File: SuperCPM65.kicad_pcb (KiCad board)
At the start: 2 copper layers, 98.5 x 79.5 mm, 36 parts, among them CON1 db_vgparts_SNES-EDGE, J1 GSD090012SEU, J2 Mini-DIN-6, J3 Conn_01x06, U1 TXB0104D, U2 W65C22NxP, U3 AP2205-33W5-7, U4 74HC14, U5 74HC595, U6 74HC595, U8 PIC12F629-IP, U9 SST39SF010

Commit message: Routing updates
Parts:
- moved C5 2.12 mm to (66.9, 70.2), turned to -90 degrees
- moved C12 0.96 mm to (83.3, 94.3), turned to -90 degrees
- moved D5 0.60 mm to (130.7, 76.7)
- moved R6 0.40 mm to (125.8, 86.3)
- moved D4 0.30 mm to (130.6, 87.3)
- moved D3 0.25 mm to (130.5, 83.5)
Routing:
- net +5V: track 0.00 -> 362.0 mm, vias 0 -> 14
- net /BA1: track 0.00 -> 101.2 mm, vias 0 -> 6
- net ~{WR}: track 0.00 -> 91.9 mm, vias 0 -> 3
- net CLK: track 0.00 -> 91.6 mm, vias 0 -> 3
- net ~{IRQ}: track 0.00 -> 79.6 mm, vias 0 -> 2
- net ~{CE_VIA}: track 0.00 -> 71.5 mm, vias 0 -> 2
- net ~{RES}: track 0.00 -> 66.0 mm, vias 0 -> 2
- net ~{CART}: track 0.00 -> 60.0 mm, vias 0 -> 3
- net /KB_DATA: track 0.00 -> 53.8 mm, vias 0 -> 2
- net /SPI_CS: track 0.00 -> 51.4 mm, vias 0 -> 2
- net /SCK: track 0.00 -> 48.0 mm, vias 0 -> 2
- net Net-(U5-SRCLK): track 0.00 -> 47.9 mm, vias 0 -> 3
- net ~{RD}: track 0.00 -> 46.4 mm, vias 0 -> 2
- net /MOSI: track 0.00 -> 44.1 mm, vias 0 -> 2
- net /MISO: track 0.00 -> 44.0 mm, vias 0 -> 2
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- added copper zone on B.Cu, net GND
- added copper zone on F.Cu, net GND

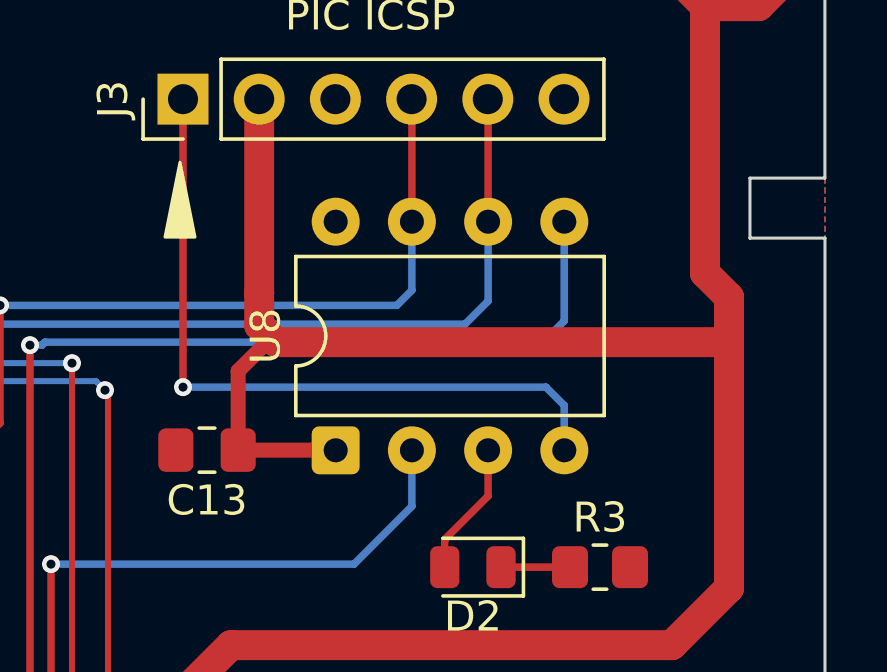
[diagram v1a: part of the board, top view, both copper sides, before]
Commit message: Fixed some 3D model issues and socketed the PIC
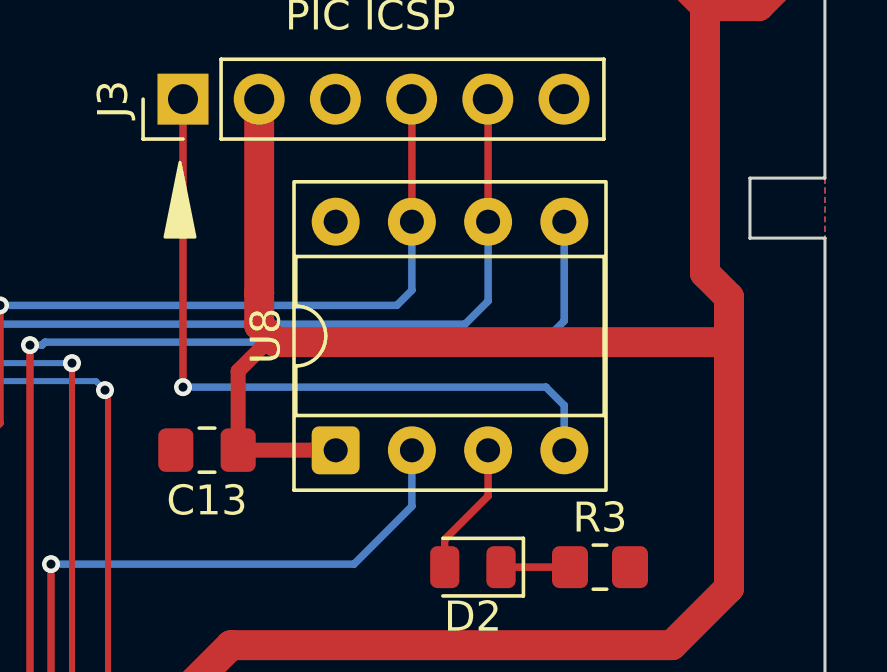
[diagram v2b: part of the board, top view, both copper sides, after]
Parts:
- U8: footprint Package_DIP:DIP-8_W7.62mm -> Package_DIP:DIP-8_W7.62mm_Socket
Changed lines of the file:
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@@
 		(property ki_fp_filters "DIP*W7.62mm* SOIC*3.9x9.9mm*P1.27mm* TSSOP*4.4x5mm*P0.65mm* SOIC*5.3x10.2mm*P1.27mm* SOIC*7.5x10.3mm*P1.27mm*")
 		(sheetname "/")
-		(sheetfile "SNES-sdcard-ps2.kicad_sch")
+		(sheetfile "SuperCPM65.kicad_sch")
 		(attr smd)
 		(fp_line
@@
 		(property ki_fp_filters "DIP*W15.24mm*")
 		(sheetname "/")
-		(sheetfile "SNES-sdcard-ps2.kicad_sch")
+		(sheetfile "SuperCPM65.kicad_sch")
 		(attr through_hole)
 		(fp_line
@@
 		(property ki_fp_filters "SOIC*14*7mm*P1.27mm*")
 		(sheetname "/")
-		(sheetfile "SNES-sdcard-ps2.kicad_sch")
+		(sheetfile "SuperCPM65.kicad_sch")
 		(attr smd)
 		(fp_line
@@
 		(property ki_fp_filters "Connector*:*_1x??_*")
 		(sheetname "/")
-		(sheetfile "SNES-sdcard-ps2.kicad_sch")
+		(sheetfile "SuperCPM65.kicad_sch")
 		(attr through_hole)
 		(fp_line
@@
 		(property ki_fp_filters "D*SOD?123*")
 		(sheetname "/")
-		(sheetfile "SNES-sdcard-ps2.kicad_sch")
+		(sheetfile "SuperCPM65.kicad_sch")
 		(attr smd)
 		(fp_line
@@
 		(property ki_fp_filters "C_*")
 		(sheetname "/")
-		(sheetfile "SNES-sdcard-ps2.kicad_sch")
+		(sheetfile "SuperCPM65.kicad_sch")
 		(attr smd)
 		(fp_line
@@
 		(property ki_fp_filters "D*SOD?123*")
 		(sheetname "/")
-		(sheetfile "SNES-sdcard-ps2.kicad_sch")
+		(sheetfile "SuperCPM65.kicad_sch")
 		(attr smd)
 		(fp_line
@@
 		(property ki_fp_filters "C_*")
 		(sheetname "/")
-		(sheetfile "SNES-sdcard-ps2.kicad_sch")
+		(sheetfile "SuperCPM65.kicad_sch")
 		(attr smd)
 		(fp_line
@@
 		(property ki_fp_filters "C_*")
 		(sheetname "/")
-		(sheetfile "SNES-sdcard-ps2.kicad_sch")
+		(sheetfile "SuperCPM65.kicad_sch")
 		(attr smd)
 		(fp_line
@@
 		)
 		(sheetname "/")
-		(sheetfile "SNES-sdcard-ps2.kicad_sch")
+		(sheetfile "SuperCPM65.kicad_sch")
 		(attr smd)
 		(fp_line
@@
 		(property ki_fp_filters "D*SOD?123*")
 		(sheetname "/")
-		(sheetfile "SNES-sdcard-ps2.kicad_sch")
+		(sheetfile "SuperCPM65.kicad_sch")
 		(attr smd)
 		(fp_line
@@
 		(property ki_fp_filters "C_*")
 		(sheetname "/")
-		(sheetfile "SNES-sdcard-ps2.kicad_sch")
+		(sheetfile "SuperCPM65.kicad_sch")
 		(attr smd)
 		(fp_line
@@
 		(property ki_fp_filters "MINI?DIN*")
 		(sheetname "/")
-		(sheetfile "SNES-sdcard-ps2.kicad_sch")
+		(sheetfile "SuperCPM65.kicad_sch")
 		(attr through_hole)
 		(fp_line
@@
 		(property ki_fp_filters "LED* LED_SMD:* LED_THT:*")
 		(sheetname "/")
-		(sheetfile "SNES-sdcard-ps2.kicad_sch")
+		(sheetfile "SuperCPM65.kicad_sch")
 		(attr smd)
 		(fp_line
@@
 		)
 	)
-	(footprint "Package_DIP:DIP-8_W7.62mm"
+	(footprint "Package_DIP:DIP-8_W7.62mm_Socket"
 		(layer "F.Cu")
 		(at 146.19 102.605 90)
-		(descr "8-lead though-hole mounted DIP package, row spacing 7.62mm (300 mils)")
-		(tags "THT DIP DIL PDIP 2.54mm 7.62mm 300mil")
+		(descr "8-lead though-hole mounted DIP package, row spacing 7.62mm (300 mils), Socket")
+		(tags "THT DIP DIL PDIP 2.54mm 7.62mm 300mil Socket")
 		(property "Reference" "U8"
 			(at 3.81 -2.33 90)
@@
 		(property "Datasheet" ""
 			(at 0 0 90)
-			(unlocked yes)
 			(layer "F.Fab")
 			(hide yes)
@@
 		(property "Description" ""
 			(at 0 0 90)
-			(unlocked yes)
 			(layer "F.Fab")
 			(hide yes)
@@
 		(property ki_fp_filters "DIP*W7.62mm*")
 		(sheetname "/")
-		(sheetfile "SNES-sdcard-ps2.kicad_sch")
+		(sheetfile "SuperCPM65.kicad_sch")
 		(attr through_hole)
 		(fp_line
@@
 			(layer "F.SilkS")
 		)
+		(fp_rect
+			(start -1.33 -1.39)
+			(end 8.95 9.01)
+			(stroke
+				(width 0.12)
+				(type solid)
+			)
+			(fill no)
+			(layer "F.SilkS")
+		)
 		(fp_arc
 			(start 4.81 -1.33)
@@
 		)
 		(fp_rect
-			(start -1.06 -1.52)
-			(end 8.67 9.14)
+			(start -1.52 -1.58)
+			(end 9.14 9.2)
 			(stroke
 				(width 0.05)
@@
 			(layer "F.Fab")
 		)
+		(fp_rect
+			(start -1.27 -1.33)
+			(end 8.89 8.95)
+			(stroke
+				(width 0.1)
+				(type solid)
+			)
+			(fill no)
+			(layer "F.Fab")
+		)
 		(fp_text user "${REFERENCE}"
-			(at 3.81 3.81 90)
+			(at 3.81 3.81 180)
 			(layer "F.Fab")
 			(effects
@@
 		)
 		(embedded_fonts no)
-		(model "${KICAD9_3DMODEL_DIR}/Package_DIP.3dshapes/DIP-8_W7.62mm.wrl"
+		(model "${KICAD9_3DMODEL_DIR}/Package_DIP.3dshapes/DIP-8_W7.62mm_Socket.wrl"
+			(hide yes)
+			(offset
+				(xyz 0 0 0)
+			)
+			(scale
+				(xyz 1 1 1)
+			)
+			(rotate
+				(xyz 0 0 0)
+			)
+		)
+		(model "${KIPRJMOD}/Local_lib/step_files/DIP-8 W7.62mm IC with Socket.stp"
 			(offset
 				(xyz 0 0 0)
@@
 		(property ki_fp_filters "C_*")
 		(sheetname "/")
-		(sheetfile "SNES-sdcard-ps2.kicad_sch")
+		(sheetfile "SuperCPM65.kicad_sch")
 		(attr smd)
 		(fp_line
@@
 		(property ki_fp_filters "D*SOD?123*")
 		(sheetname "/")
-		(sheetfile "SNES-sdcard-ps2.kicad_sch")
+		(sheetfile "SuperCPM65.kicad_sch")
 		(attr smd)
 		(fp_line
@@
 		(property ki_fp_filters "DIP*W7.62mm* SOIC*3.9x9.9mm*P1.27mm* TSSOP*4.4x5mm*P0.65mm* SOIC*5.3x10.2mm*P1.27mm* SOIC*7.5x10.3mm*P1.27mm*")
 		(sheetname "/")
-		(sheetfile "SNES-sdcard-ps2.kicad_sch")
+		(sheetfile "SuperCPM65.kicad_sch")
 		(attr smd)
 		(fp_line
@@
 		(property ki_fp_filters "C_*")
 		(sheetname "/")
-		(sheetfile "SNES-sdcard-ps2.kicad_sch")
+		(sheetfile "SuperCPM65.kicad_sch")
 		(attr smd)
 		(fp_line
@@
 		(property ki_fp_filters "SOT?23?5*")
 		(sheetname "/")
-		(sheetfile "SNES-sdcard-ps2.kicad_sch")
+		(sheetfile "SuperCPM65.kicad_sch")
 		(attr smd)
 		(fp_line
@@
 		(property ki_fp_filters "D*SOD?123*")
 		(sheetname "/")
-		(sheetfile "SNES-sdcard-ps2.kicad_sch")
+		(sheetfile "SuperCPM65.kicad_sch")
 		(attr smd)
 		(fp_line
@@
 		(property ki_fp_filters "R_*")
 		(sheetname "/")
-		(sheetfile "SNES-sdcard-ps2.kicad_sch")
+		(sheetfile "SuperCPM65.kicad_sch")
 		(attr smd)
 		(fp_line
@@
 		(property ki_fp_filters "R_*")
 		(sheetname "/")
-		(sheetfile "SNES-sdcard-ps2.kicad_sch")
+		(sheetfile "SuperCPM65.kicad_sch")
 		(attr smd)
 		(fp_line
@@
 		(property ki_fp_filters "R_*")
 		(sheetname "/")
-		(sheetfile "SNES-sdcard-ps2.kicad_sch")
+		(sheetfile "SuperCPM65.kicad_sch")
 		(attr smd)
 		(fp_line
@@
 		(property ki_fp_filters "C_*")
 		(sheetname "/")
-		(sheetfile "SNES-sdcard-ps2.kicad_sch")
+		(sheetfile "SuperCPM65.kicad_sch")
 		(attr smd)
 		(fp_line
@@
 		)
 		(sheetname "/")
-		(sheetfile "SNES-sdcard-ps2.kicad_sch")
+		(sheetfile "SuperCPM65.kicad_sch")
 		(attr through_hole exclude_from_bom)
 		(fp_circle
@@
 		(property ki_fp_filters "C_*")
 		(sheetname "/")
-		(sheetfile "SNES-sdcard-ps2.kicad_sch")
+		(sheetfile "SuperCPM65.kicad_sch")
 		(attr smd)
 		(fp_line
@@
 		(property ki_fp_filters "C_*")
 		(sheetname "/")
-		(sheetfile "SNES-sdcard-ps2.kicad_sch")
+		(sheetfile "SuperCPM65.kicad_sch")
 		(attr smd)
 		(fp_line
@@
 		(property ki_fp_filters "C_*")
 		(sheetname "/")
-		(sheetfile "SNES-sdcard-ps2.kicad_sch")
+		(sheetfile "SuperCPM65.kicad_sch")
 		(attr smd)
 		(fp_line
@@
 		(property ki_fp_filters "R_*")
 		(sheetname "/")
-		(sheetfile "SNES-sdcard-ps2.kicad_sch")
+		(sheetfile "SuperCPM65.kicad_sch")
 		(attr smd)
 		(fp_line
@@
 		)
 		(sheetname "/")
-		(sheetfile "SNES-sdcard-ps2.kicad_sch")
+		(sheetfile "SuperCPM65.kicad_sch")
 		(attr through_hole)
 		(fp_line
@@
 		)
 		(model "/home/venomix/KiCadProjects/dipstep/DIP-32 W15.24mm IC with Socket.stp"
+			(hide yes)
+			(offset
+				(xyz 0 0 0)
+			)
+			(scale
+				(xyz 1 1 1)
+			)
+			(rotate
+				(xyz -0 -0 90)
+			)
+		)
+		(model "${KIPRJMOD}/Local_lib/step_files/DIP-32 W15.24mm IC with Socket.stp"
 			(offset
 				(xyz 0 0 0)
@@
 		(property ki_fp_filters "DIP*W7.62mm*")
 		(sheetname "/")
-		(sheetfile "SNES-sdcard-ps2.kicad_sch")
+		(sheetfile "SuperCPM65.kicad_sch")
 		(attr smd)
 		(fp_line
@@
 		(property ki_fp_filters "R_*")
 		(sheetname "/")
-		(sheetfile "SNES-sdcard-ps2.kicad_sch")
+		(sheetfile "SuperCPM65.kicad_sch")
 		(attr smd)
 		(fp_line
@@
 		(property ki_fp_filters "C_*")
 		(sheetname "/")
-		(sheetfile "SNES-sdcard-ps2.kicad_sch")
+		(sheetfile "SuperCPM65.kicad_sch")
 		(attr smd)
 		(fp_line
@@
 		(property ki_fp_filters "C_*")
 		(sheetname "/")
-		(sheetfile "SNES-sdcard-ps2.kicad_sch")
+		(sheetfile "SuperCPM65.kicad_sch")
 		(attr smd)
 		(fp_line

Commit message: Continued routing, more or less completed
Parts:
- added D5: LED, LED_SMD:LED_0805_2012Metric, F.Cu at (82.3, 101.0)
- added D6: LED, LED_SMD:LED_0805_2012Metric, F.Cu at (123.1, 68.2)
- added J1: Conn_01x02, Connector_PinHeader_2.54mm:PinHeader_1x02_P2.54mm_Vertical, F.Cu at (76.2, 96.3)
- added J3: Conn_01x06, Connector_PinHeader_2.54mm:PinHeader_1x06_P2.54mm_Vertical, F.Cu at (105.0, 46.8)
- added R3: 10k, Resistor_SMD:R_0805_2012Metric_Pad1.20x1.40mm_HandSolder, F.Cu at (76.2, 91.4)
- added R4: 1k, Resistor_SMD:R_0805_2012Metric_Pad1.20x1.40mm_HandSolder, F.Cu at (82.3, 104.3)
- added R5: 1k, Resistor_SMD:R_0805_2012Metric_Pad1.20x1.40mm_HandSolder, F.Cu at (123.1, 70.4)
- moved G*** 6.17 mm to (77.7, 48.8)
- moved J5 0.20 mm to (116.5, 42.2)
- moved J4 0.10 mm to (142.4, 54.8)
- renumbered C13 to C1, C4 to C10, C9 to C11, C10 to C12, C12 to C2, C5 to C3, C6 to C4, C3 to C5, C2 to C6, C11 to C7, C7 to C8, C8 to C9, D3 to D1, D5 to D2, D4 to D3, D6 to D4, D2 to D7, D1 to D8, J3 to J2, J1 to J4, J2 to J5, R6 to R1, R7 to R2, R3 to R6, R1 to R7, R2 to R8, U4 to U1, U8 to U2, U9 to U3, U2 to U4, U1 to U7, U3 to U8
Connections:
- CON1 pad 43: unconnected-(CON1-BA2-Pad43) -> /BA2
- CON1 pad 44: unconnected-(CON1-BA3-Pad44) -> /BA3
- D3 pad 2: /BA1 -> /BA3
- U1 pad 10: unconnected-(U4-Pad10) -> Net-(D5-A)
- U1 pad 11: GND -> ~{CE_ROM}
- U1 pad 12: unconnected-(U4-Pad12) -> Net-(D6-A)
- U1 pad 13: GND -> ~{CE_VIA}
- U1 pad 9: /BA1 -> /BA3
- U3 pad 1: unconnected-(U9-NC-Pad1) -> /BA2
- U3 pad 30: unconnected-(U9-NC-Pad30) -> /BA1
- U3 pad 31: +5V -> Net-(J1-Pin_1)
- U4 pad 2: unconnected-(U2-PA0-Pad2) -> /PA0
- U4 pad 7: unconnected-(U2-PA5-Pad7) -> /PA5
- U4 pad 8: unconnected-(U2-PA6-Pad8) -> /PA6
- U4 pad 9: unconnected-(U2-PA7-Pad9) -> /PA7
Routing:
- net /BA3: track 0.00 -> 95.4 mm, vias 0 -> 5
- net Net-(D5-A): track 0.00 -> 71.6 mm, vias 0 -> 4
- net /BA1: track 101.2 -> 32.4 mm, vias 6 -> 3
- net GND: track 16.1 -> 63.0 mm, vias 3 -> 38
- net /PA0: track 0.00 -> 36.7 mm, vias 0 -> 1
- net /BA2: track 0.00 -> 33.4 mm, vias 0 -> 3
- net ~{CE_ROM}: track 25.7 -> 55.8 mm, vias 2 -> 4
- net /PA5: track 0.00 -> 27.0 mm, vias 0 -> 1
- net /PA7: track 0.00 -> 25.7 mm, vias 0 -> 2
- net Net-(U4-CB1): track 27.5 -> 53.1 mm, vias 2 -> 3
- net /PA6: track 0.00 -> 25.3 mm, vias 0 -> 1
- net Net-(J1-Pin_1): track 0.00 -> 21.1 mm, vias 0 -> 1
- net ~{CE_VIA}: track 71.5 -> 85.4 mm, vias 2 -> 4
- net Net-(D6-A): track 0.00 -> 7.19 mm
- net Net-(D5-K): track 0.00 -> 3.34 mm
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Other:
- board text added: "CIC OK"
- board text added: "ROM CE"
- board text added: "ROM WE"
- board text added: "VIA CE"

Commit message: Added stitching vias to improve ground plane impedance and fill ratio
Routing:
- net GND: vias 38 -> 65
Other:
- board text added: "SUPER CP/M-65 PCB REV A"
- board text removed: "SUPER CP/M 65 PCB REV A"
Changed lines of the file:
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@@
 		(layer "F.SilkS")
 	)
-	(gr_text "SUPER CP/M 65 \nPCB REV A"
+	(gr_text "SUPER CP/M-65 \nPCB REV A"
 		(at 66.2 109.6 0)
 		(layer "F.SilkS")
@@
 	)
 	(via
+		(at 160.8 52.4)
+		(size 0.6)
+		(drill 0.3)
+		(layers "F.Cu" "B.Cu")
+		(free yes)
+		(net 1)
+	)
+	(via
 		(at 94.2 66.3)
 		(size 0.6)
@@
 	)
 	(via
+		(at 65.5 49.9)
+		(size 0.6)
+		(drill 0.3)
+		(layers "F.Cu" "B.Cu")
+		(free yes)
+		(net 1)
+	)
+	(via
 		(at 80.7 76.7)
 		(size 0.6)
@@
 	)
 	(via
+		(at 141.6 85.6)
+		(size 0.6)
+		(drill 0.3)
+		(layers "F.Cu" "B.Cu")
+		(free yes)
+		(net 1)
+	)
+	(via
+		(at 65.5 51.1)
+		(size 0.6)
+		(drill 0.3)
+		(layers "F.Cu" "B.Cu")
+		(free yes)
+		(net 1)
+	)
+	(via
 		(at 73 80.1)
 		(size 0.6)
@@
 	)
 	(via
+		(at 110.7 87.2)
+		(size 0.6)
+		(drill 0.3)
+		(layers "F.Cu" "B.Cu")
+		(free yes)
+		(net 1)
+	)
+	(via
+		(at 90.6 98.6)
+		(size 0.6)
+		(drill 0.3)
+		(layers "F.Cu" "B.Cu")
+		(free yes)
+		(net 1)
+	)
+	(via
+		(at 87.3 87.1)
+		(size 0.6)
+		(drill 0.3)
+		(layers "F.Cu" "B.Cu")
+		(free yes)
+		(net 1)
+	)
+	(via
+		(at 160.8 54)
+		(size 0.6)
+		(drill 0.3)
+		(layers "F.Cu" "B.Cu")
+		(free yes)
+		(net 1)
+	)
+	(via
 		(at 142.1 75.4)
 		(size 0.6)
@@
 	)
 	(via
+		(at 94.9 87.2)
+		(size 0.6)
+		(drill 0.3)
+		(layers "F.Cu" "B.Cu")
+		(free yes)
+		(net 1)
+	)
+	(via
 		(at 81 109.4)
 		(size 0.6)
@@
 	)
 	(via
+		(at 140.2 85.6)
+		(size 0.6)
+		(drill 0.3)
+		(layers "F.Cu" "B.Cu")
+		(free yes)
+		(net 1)
+	)
+	(via
+		(at 113.2 86.7)
+		(size 0.6)
+		(drill 0.3)
+		(layers "F.Cu" "B.Cu")
+		(free yes)
+		(net 1)
+	)
+	(via
+		(at 100.7 87.2)
+		(size 0.6)
+		(drill 0.3)
+		(layers "F.Cu" "B.Cu")
+		(free yes)
+		(net 1)
+	)
+	(via
 		(at 139.5 102.6)
 		(size 0.6)
@@
 	)
 	(via
+		(at 137.2 85.6)
+		(size 0.6)
+		(drill 0.3)
+		(layers "F.Cu" "B.Cu")
+		(free yes)
+		(net 1)
+	)
+	(via
+		(at 132.3 91.6)
+		(size 0.6)
+		(drill 0.3)
+		(layers "F.Cu" "B.Cu")
+		(free yes)
+		(net 1)
+	)
+	(via
 		(at 84.1 76.7)
 		(size 0.6)
@@
 	)
 	(via
+		(at 138.7 85.6)
+		(size 0.6)
+		(drill 0.3)
+		(layers "F.Cu" "B.Cu")
+		(free yes)
+		(net 1)
+	)
+	(via
 		(at 83.3 97.2)
 		(size 0.6)
@@
 	)
 	(via
+		(at 160.8 50.9)
+		(size 0.6)
+		(drill 0.3)
+		(layers "F.Cu" "B.Cu")
+		(free yes)
+		(net 1)
+	)
+	(via
+		(at 108.2 87.2)
+		(size 0.6)
+		(drill 0.3)
+		(layers "F.Cu" "B.Cu")
+		(free yes)
+		(net 1)
+	)
+	(via
 		(at 160.2 73.8)
 		(size 0.6)
@@
 	)
 	(via
+		(at 103.5 87.2)
+		(size 0.6)
+		(drill 0.3)
+		(layers "F.Cu" "B.Cu")
+		(free yes)
+		(net 1)
+	)
+	(via
 		(at 66.9 73)
 		(size 0.6)
@@
 	)
 	(via
+		(at 65.5 52.4)
+		(size 0.6)
+		(drill 0.3)
+		(layers "F.Cu" "B.Cu")
+		(free yes)
+		(net 1)
+	)
+	(via
+		(at 84.8 87.1)
+		(size 0.6)
+		(drill 0.3)
+		(layers "F.Cu" "B.Cu")
+		(free yes)
+		(net 1)
+	)
+	(via
 		(at 84.8 104.3)
 		(size 0.6)
@@
 	)
 	(via
+		(at 89.8 87)
+		(size 0.6)
+		(drill 0.3)
+		(layers "F.Cu" "B.Cu")
+		(free yes)
+		(net 1)
+	)
+	(via
 		(at 79.9 109.4)
 		(size 0.6)
@@
 	)
 	(via
+		(at 98 87.2)
+		(size 0.6)
+		(drill 0.3)
+		(layers "F.Cu" "B.Cu")
+		(free yes)
+		(net 1)
+	)
+	(via
+		(at 160.8 55.5)
+		(size 0.6)
+		(drill 0.3)
+		(layers "F.Cu" "B.Cu")
+		(free yes)
+		(net 1)
+	)
+	(via
 		(at 161 105.1)
 		(size 0.6)
@@
 		(size 0.6)
 		(drill 0.3)
+		(layers "F.Cu" "B.Cu")
+		(free yes)
+		(net 1)
+	)
+	(via
+		(at 92.4 87.3)
+		(size 0.6)
+		(drill 0.3)
+		(layers "F.Cu" "B.Cu")
+		(free yes)
+		(net 1)
+	)
+	(via
+		(at 90.5 103.1)
+		(size 0.6)
+		(drill 0.3)
+		(layers "F.Cu" "B.Cu")
+		(free yes)
+		(net 1)
+	)
+	(via
+		(at 92.1 94.9)
+		(size 0.6)
+		(drill 0.3)
+		(layers "F.Cu" "B.Cu")
+		(free yes)
+		(net 1)
+	)
+	(via
+		(at 106 87.2)
+		(size 0.6)
+		(drill 0.3)

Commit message: Silkscreen cleanup etc.
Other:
- board text added: "+5V"
- board text added: "GND"
- board text added: "PA0"
- board text added: "PA5"
- board text added: "PA6"
- board text added: "PA7"
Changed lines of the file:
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@@
 			(outputformat 1)
 			(mirror no)
-			(drillshape 1)
+			(drillshape 0)
 			(scaleselection 1)
-			(outputdirectory "")
+			(outputdirectory "Gerber/")
 		)
 	)
@@
 		(layer "F.SilkS")
 	)
+	(gr_text "PA0"
+		(at 103.2 51.3 90)
+		(layer "F.SilkS")
+		(effects
+			(font
+				(size 1 1)
+				(thickness 0.1)
+			)
+			(justify left bottom)
+		)
+	)
 	(gr_text "SUPER CP/M-65 \nPCB REV A"
 		(at 66.2 109.6 0)
@@
 		)
 	)
+	(gr_text "PA6"
+		(at 98.5 53.5 90)
+		(layer "F.SilkS")
+		(effects
+			(font
+				(size 1 1)
+				(thickness 0.1)
+			)
+			(justify left bottom)
+		)
+	)
 	(gr_text "VIA CE"
 		(at 125.7 69.8 0)
@@
 		)
 	)
+	(gr_text "PA7"
+		(at 95.6 53.6 90)
+		(layer "F.SilkS")
+		(effects
+			(font
+				(size 1 1)
+				(thickness 0.1)
+			)
+			(justify left bottom)
+		)
+	)
+	(gr_text "PA5"
+		(at 100.5 51.3 90)
+		(layer "F.SilkS")
+		(effects
+			(font
+				(size 1 1)
+				(thickness 0.1)
+			)
+			(justify left bottom)
+		)
+	)
+	(gr_text "+5V"
+		(at 105.7 51.8 90)
+		(layer "F.SilkS")
+		(effects
+			(font
+				(size 1 1)
+				(thickness 0.1)
+			)
+			(justify left bottom)
+		)
+	)
 	(gr_text "ROM WE"
 		(at 79.6 100.5 90)
@@
 		)
 	)
+	(gr_text "GND"
+		(at 92.9 51.5 90)
+		(layer "F.SilkS")
+		(effects
+			(font
+				(size 1 1)
+				(thickness 0.1)
+			)
+			(justify left bottom)
+		)
+	)
 	(gr_text "ROM CE"
 		(at 74.2 103.2 0)
@@
 		)
 	)
+	(dimension
+		(type aligned)
+		(layer "Dwgs.User")
+		(pts
+			(xy 88.2 121.5) (xy 88.2 42)
+		)
+		(height -36.5)
+		(format
+			(prefix "")
+			(suffix "")
+			(units 3)
+			(units_format 0)
+			(precision 4)
+			(suppress_zeroes yes)
+		)
+		(style
+			(thickness 0.1)
+			(arrow_length 1.27)
+			(text_position_mode 0)
+			(arrow_direction outward)
+			(extension_height 0.58642)
+			(extension_offset 0.5)
+			(keep_text_aligned yes)
+		)
+		(gr_text "79,5"
+			(at 50.55 81.75 90)
+			(layer "Dwgs.User")
+			(effects
+				(font
+					(size 1 1)
+					(thickness 0.15)
+				)
+			)
+		)
+	)
+	(dimension
+		(type aligned)
+		(layer "Dwgs.User")
+		(pts
+			(xy 64.0005 43.99913) (xy 162.49916 43.99913)
+		)
+		(height -6.49913)
+		(format
+			(prefix "")
+			(suffix "")
+			(units 3)
+			(units_format 0)
+			(precision 4)
+			(suppress_zeroes yes)
+		)
+		(style
+			(thickness 0.1)
+			(arrow_length 1.27)
+			(text_position_mode 0)
+			(arrow_direction outward)
+			(extension_height 0.58642)
+			(extension_offset 0.5)
+			(keep_text_aligned yes)
+		)
+		(gr_text "98,4987"
+			(at 113.24983 36.35 0)
+			(layer "Dwgs.User")
+			(effects
+				(font
+					(size 1 1)
+					(thickness 0.15)
+				)
+			)
+		)
+	)
